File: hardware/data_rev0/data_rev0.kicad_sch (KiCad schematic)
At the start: 22 parts, among them J1 AudioJack3, J2 AudioJack3, J3 BOARD, SW3 PTS636, U1 CAP1206-x-AIA, U2 Pico

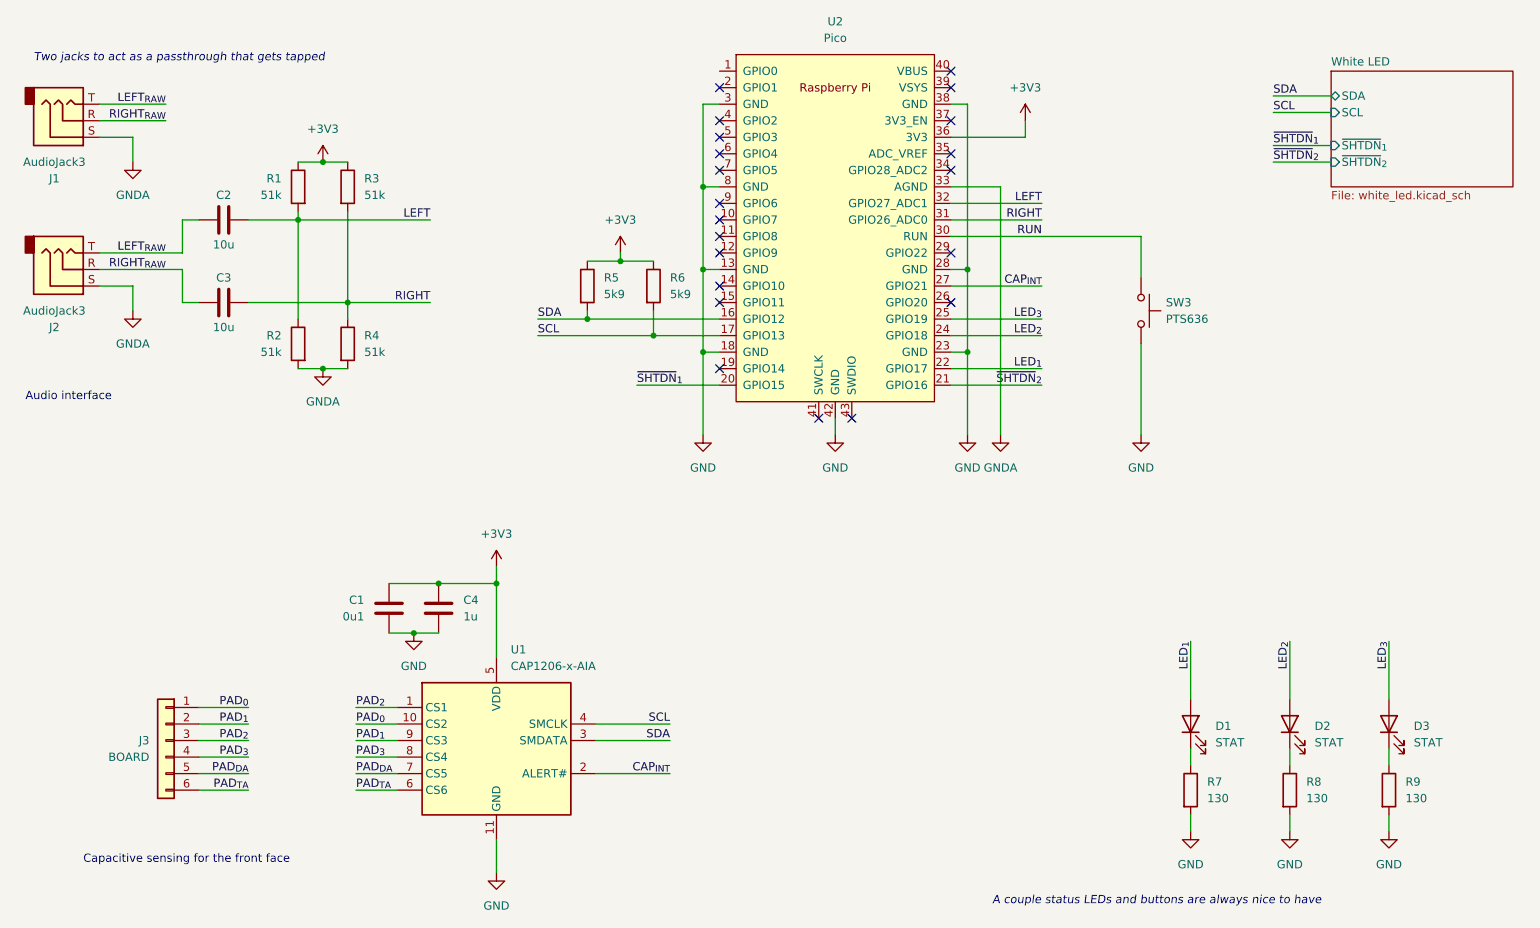
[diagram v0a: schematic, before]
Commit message: Added Rev 0 project
Started some of my changes on Rev 1. Also changed the RP Pico footprint to have solderpaste on the pads.
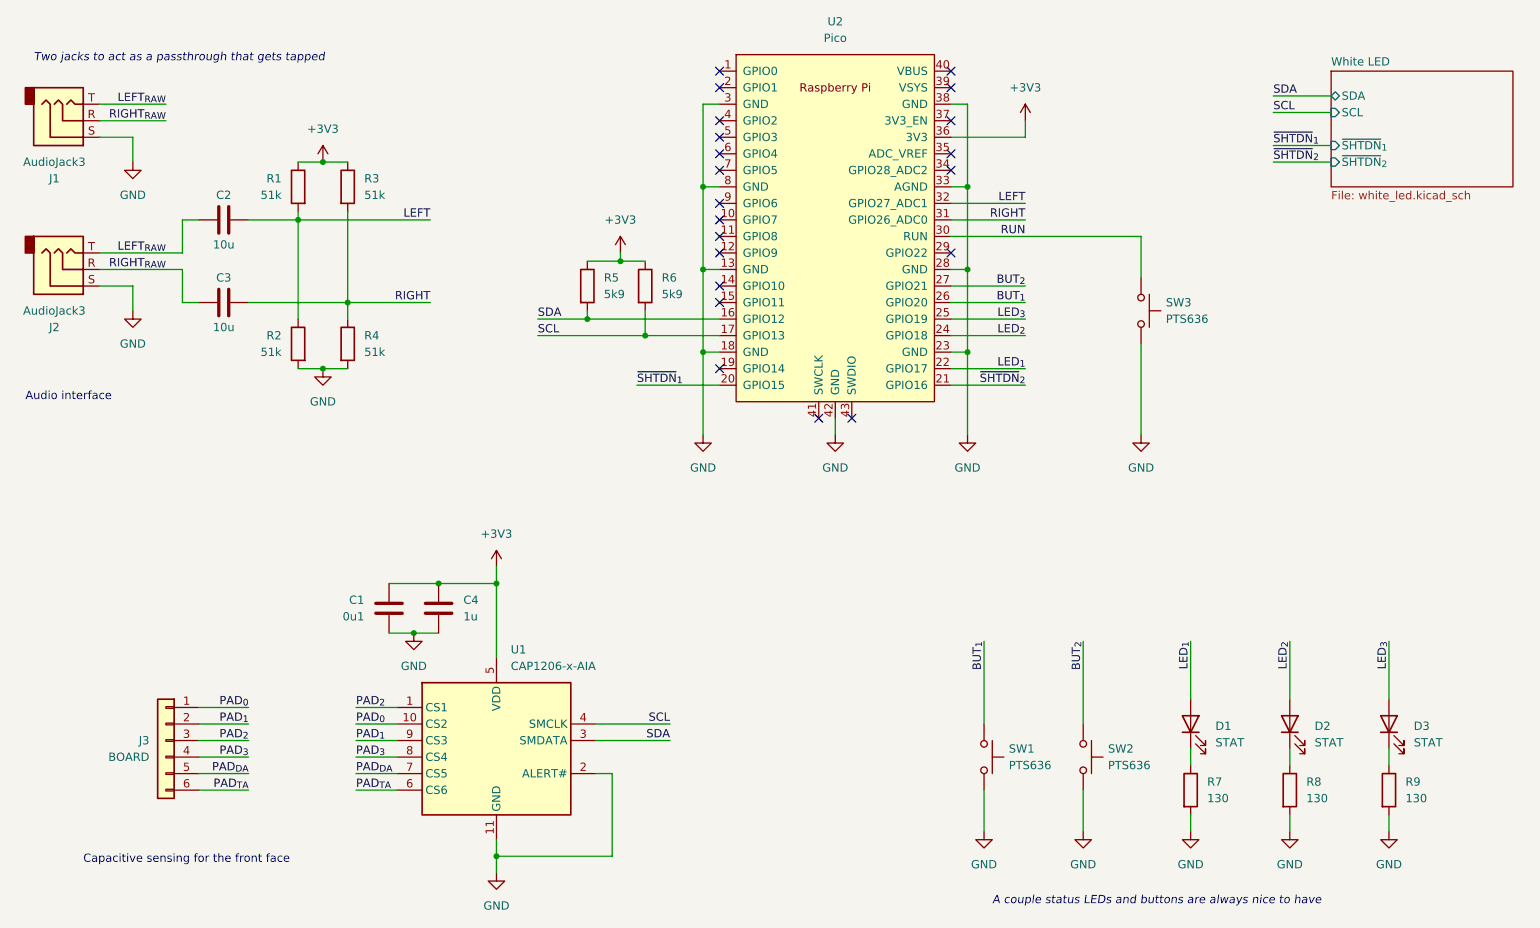
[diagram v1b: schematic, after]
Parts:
- added SW1, SW2: PTS636, Button_Switch_SMD:SW_SPST_CK_RS282G05A3, symbol Switch:SW_Push
- U2: footprint RPi_Pico:RPi_Pico_SMD_TH -> RPi_Pico:RPi_Pico_SMD
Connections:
- net GNDA is gone; now on net GND: J1.S, J2.S, R2.2, R4.2, U2.33 (AGND)
- net GND: now also U1.2 (ALERT#), SW1.2, SW2.2
- net BUT_{1}: now reaches U2.26 (GPIO20)
- net BUT_{1}: now also SW1.1
- net CAP_{INT} renamed BUT_{2}
- net BUT_{2}: now also SW2.1; no longer U1.2 (ALERT#)
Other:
- moved on the sheet: R6
